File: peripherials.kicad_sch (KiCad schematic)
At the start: 58 parts, among them U15 PN7160AHN

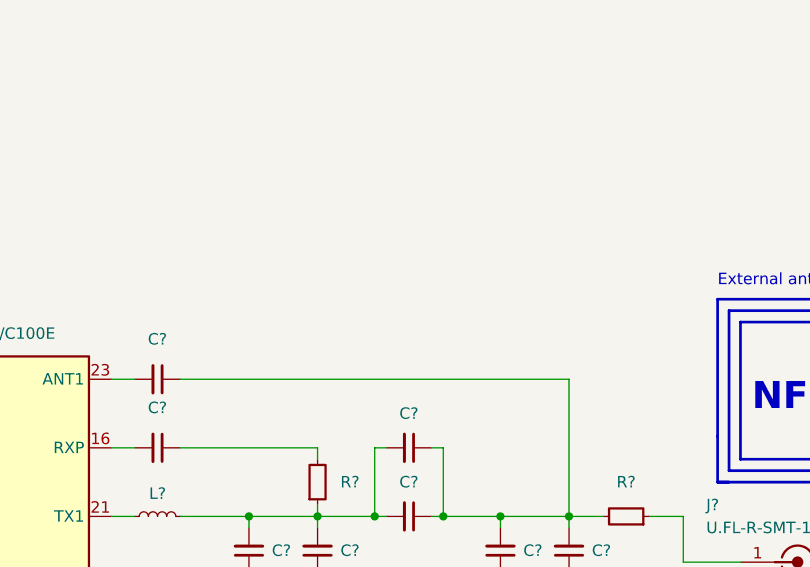
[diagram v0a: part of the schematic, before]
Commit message: [#54617] NFC: mark matching network as DNP & add note about it
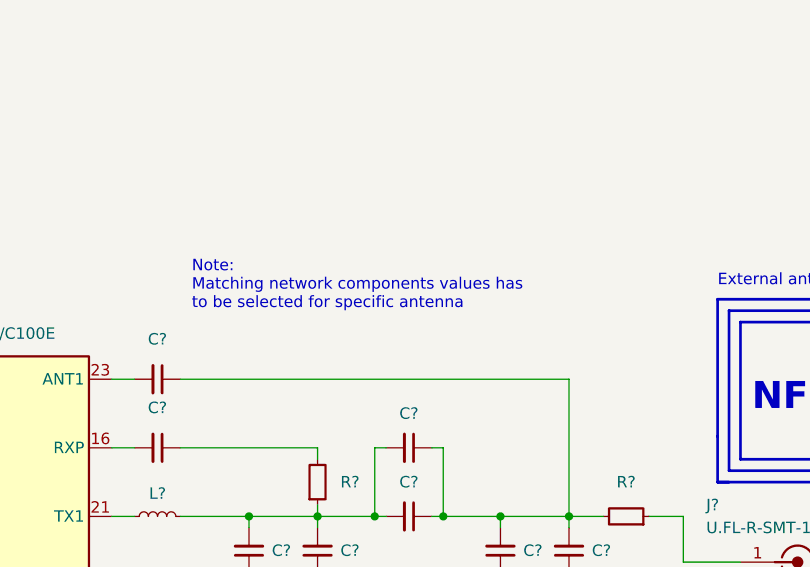
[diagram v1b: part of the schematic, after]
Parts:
- C? (x16), R? (x4): DNP (none) -> DNP
- L? (x2): footprint antmicro-footprints:L_0402_1005Metric -> antmicro-footprints:L_0603_1608Metric
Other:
- note added: "Note: Matching network components values has to be selected for specific antenna"
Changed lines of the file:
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@@
     (effects (font (size 1.27 1.27)) (justify left bottom))
   )
+  (text "Note:\nMatching network components values has \nto be selected for specific antenna"
+    (at 316.23 85.09 0)
+    (effects (font (size 1.27 1.27)) (justify left bottom))
+  )
   (text "GPIO connector" (at 19.05 153.67 0)
     (effects (font (size 2.9972 2.9972) (thickness 0.5994) bold) (justify left bottom))
@@
       (effects (font (size 1.27 1.27)) (justify left bottom) hide)
     )
+    (property "DNP" "DNP" (id 10) (at 367.03 123.19 0)
+      (effects (font (size 1.27 1.27)) hide)
+    )
     (pin "1")
     (pin "2")
@@
       (effects (font (size 1.27 1.27)) (justify left bottom) hide)
     )
+    (property "DNP" "DNP" (id 11) (at 342.9 100.33 0)
+      (effects (font (size 1.27 1.27)) hide)
+    )
     (pin "1")
     (pin "2")
@@
       (effects (font (size 1.27 1.27)) (justify left bottom) hide)
     )
+    (property "DNP" "DNP" (id 11) (at 342.9 107.95 0)
+      (effects (font (size 1.27 1.27)) hide)
+    )
     (pin "1")
     (pin "2")
@@
       (effects (font (size 1.27 1.27)) (justify left bottom) hide)
     )
+    (property "DNP" "DNP" (id 11) (at 322.58 121.92 0)
+      (effects (font (size 1.27 1.27)) hide)
+    )
     (pin "1")
     (pin "2")
@@
       (effects (font (size 1.27 1.27)) (justify left bottom) hide)
     )
+    (property "DNP" "DNP" (id 11) (at 342.9 130.81 0)
+      (effects (font (size 1.27 1.27)) hide)
+    )
     (pin "1")
     (pin "2")
@@
       (effects (font (size 1.27 1.27)) (justify left bottom) hide)
     )
+    (property "DNP" "DNP" (id 10) (at 330.2 106.68 0)
+      (effects (font (size 1.27 1.27)) hide)
+    )
     (pin "1")
     (pin "2")
@@
       (effects (font (size 1.27 1.27)) (justify left bottom) hide)
     )
+    (property "DNP" "DNP" (id 11) (at 330.2 114.3 0)
+      (effects (font (size 1.27 1.27)) hide)
+    )
     (pin "1")
     (pin "2")
@@
       (effects (font (size 1.27 1.27) (thickness 0.15)) (justify left bottom) hide)
     )
-    (property "Footprint" "antmicro-footprints:L_0402_1005Metric" (id 2) (at 323.85 130.81 0)
+    (property "Footprint" "antmicro-footprints:L_0603_1608Metric" (id 2) (at 323.85 130.81 0)
       (effects (font (size 1.27 1.27) (thickness 0.15)) (justify left bottom) hide)
     )
@@
       (effects (font (size 1.27 1.27)) (justify left bottom) hide)
     )
+    (property "DNP" "DNP" (id 11) (at 314.96 92.71 0)
+      (effects (font (size 1.27 1.27)) hide)
+    )
     (pin "1")
     (pin "2")
@@
       (effects (font (size 1.27 1.27)) (justify left bottom) hide)
     )
+    (property "DNP" "DNP" (id 11) (at 330.2 121.92 0)
+      (effects (font (size 1.27 1.27)) hide)
+    )
     (pin "1")
     (pin "2")
@@
       (effects (font (size 1.27 1.27)) (justify left bottom) hide)
     )
+    (property "DNP" "DNP" (id 11) (at 358.14 121.92 0)
+      (effects (font (size 1.27 1.27)) hide)
+    )
     (pin "1")
     (pin "2")
@@
       (effects (font (size 1.27 1.27)) (justify left bottom) hide)
     )
+    (property "DNP" "DNP" (id 10) (at 367.03 107.95 0)
+      (effects (font (size 1.27 1.27)) hide)
+    )
     (pin "1")
     (pin "2")
@@
       (effects (font (size 1.27 1.27) (thickness 0.15)) (justify left bottom) hide)
     )
-    (property "Footprint" "antmicro-footprints:L_0402_1005Metric" (id 2) (at 323.85 115.57 0)
+    (property "Footprint" "antmicro-footprints:L_0603_1608Metric" (id 2) (at 323.85 115.57 0)
       (effects (font (size 1.27 1.27) (thickness 0.15)) (justify left bottom) hide)
     )
@@
       (effects (font (size 1.27 1.27)) (justify left bottom) hide)
     )
+    (property "DNP" "DNP" (id 11) (at 314.96 138.43 0)
+      (effects (font (size 1.27 1.27)) hide)
+    )
     (pin "1")
     (pin "2")
@@
       (effects (font (size 1.27 1.27)) (justify left bottom) hide)
     )
+    (property "DNP" "DNP" (id 11) (at 350.52 121.92 0)
+      (effects (font (size 1.27 1.27)) hide)
+    )
     (pin "1")
     (pin "2")
@@
       (effects (font (size 1.27 1.27)) (justify left bottom) hide)
     )
+    (property "DNP" "DNP" (id 11) (at 314.96 130.81 0)
+      (effects (font (size 1.27 1.27)) hide)
+    )
     (pin "1")
     (pin "2")
@@
       (effects (font (size 1.27 1.27)) (justify left bottom) hide)
     )
+    (property "DNP" "DNP" (id 10) (at 330.2 124.46 0)
+      (effects (font (size 1.27 1.27)) hide)
+    )
     (pin "1")
     (pin "2")
@@
       (effects (font (size 1.27 1.27)) (justify left bottom) hide)
     )
+    (property "DNP" "DNP" (id 11) (at 358.14 114.3 0)
+      (effects (font (size 1.27 1.27)) hide)
+    )
     (pin "1")
     (pin "2")
@@
       (effects (font (size 1.27 1.27)) (justify left bottom) hide)
     )
+    (property "DNP" "DNP" (id 11) (at 342.9 123.19 0)
+      (effects (font (size 1.27 1.27)) hide)
+    )
     (pin "1")
     (pin "2")
@@
       (effects (font (size 1.27 1.27)) (justify left bottom) hide)
     )
+    (property "DNP" "DNP" (id 11) (at 314.96 100.33 0)
+      (effects (font (size 1.27 1.27)) hide)
+    )
     (pin "1")
     (pin "2")
@@
       (effects (font (size 1.27 1.27)) (justify left bottom) hide)
     )
+    (property "DNP" "DNP" (id 11) (at 350.52 114.3 0)
+      (effects (font (size 1.27 1.27)) hide)
+    )
     (pin "1")
     (pin "2")
@@
       (effects (font (size 1.27 1.27)) (justify left bottom) hide)
     )
+    (property "DNP" "DNP" (id 11) (at 322.58 114.3 0)
+      (effects (font (size 1.27 1.27)) hide)
+    )
     (pin "1")

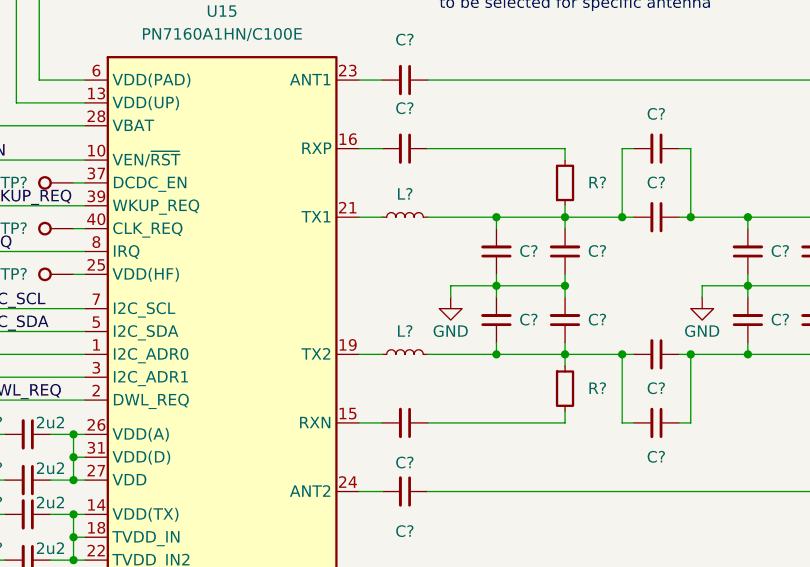
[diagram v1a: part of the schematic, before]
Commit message: [#54617] Migrate to KiCad 7
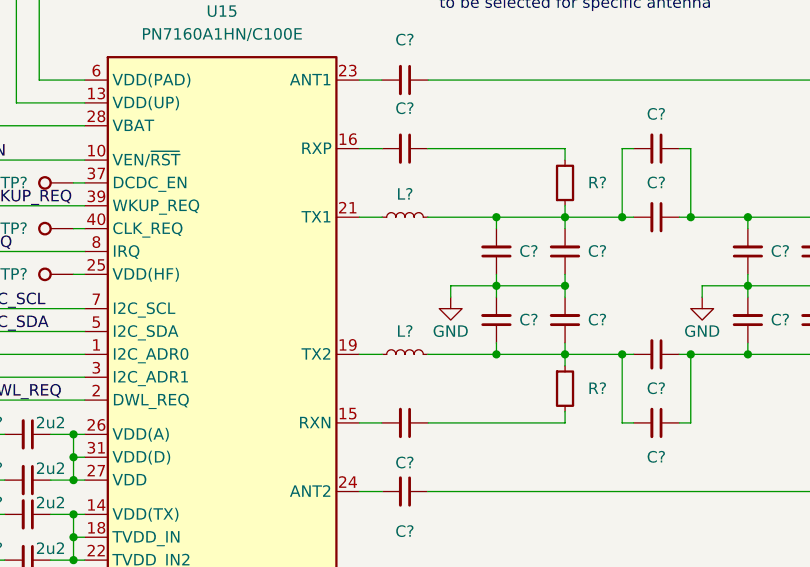
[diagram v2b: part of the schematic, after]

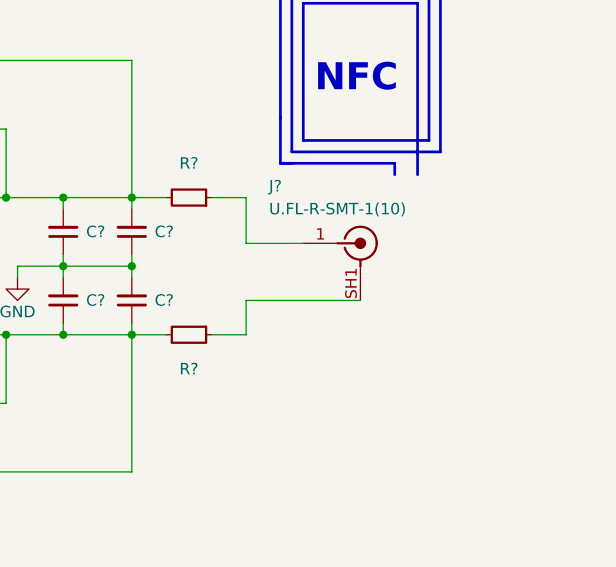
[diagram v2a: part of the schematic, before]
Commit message: [#54617] Move LVDS display related components to separate repo
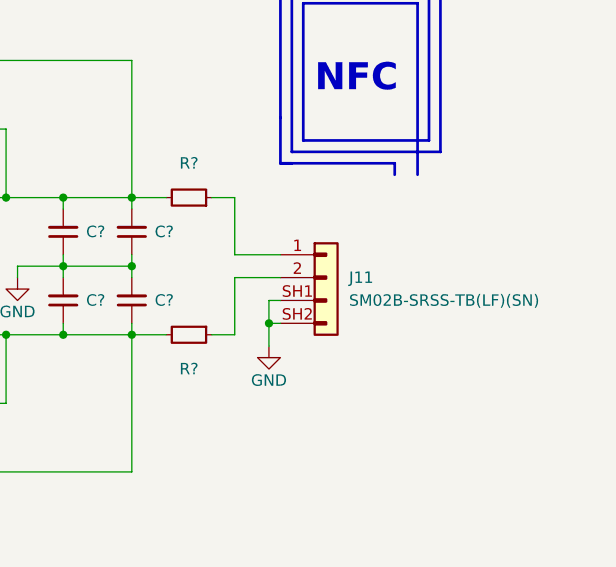
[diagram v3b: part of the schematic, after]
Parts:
- removed J?: U_FL-R-SMT-1, antmicro-footprints:Coax_Conn_U.FL, symbol antmicroCoaxialConnectorsRF:U_FL-R-SMT-1
- added J11: JST_SH_1x2_SM02B-SRSS-TB-LF-SN, antmicro-footprints:Conn_JST_SH_1x2_SM02B-SRSS-TB-LF-SN, symbol antmicroWire2BoardConnectors:JST_SH_1x2_SM02B-SRSS-TB-LF-SN
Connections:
- net GND: now also J11.SH1, J11.SH2
- net at R?.1: now also J11.2
- net at R?.1: now also J11.1
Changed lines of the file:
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@@
   (junction (at 106.68 50.8) (diameter 0) (color 0 0 0 0)
   )
+  (junction (at 373.38 121.92) (diameter 0) (color 0 0 0 0)
+  )
   (junction (at 151.13 49.53) (diameter 0) (color 0 0 0 0)
   )
@@
     (stroke (width 0) (type default))
   )
-  (wire (pts (xy 370.84 113.03) (xy 377.19 113.03))
+  (wire (pts (xy 369.57 114.3) (xy 374.65 114.3))
     (stroke (width 0) (type default))
   )
@@
     (stroke (width 0) (type default))
   )
+  (wire (pts (xy 373.38 121.92) (xy 373.38 124.46))
+    (stroke (width 0) (type default))
+  )
   (bus (pts (xy 76.2 168.91) (xy 24.13 168.91))
     (stroke (width 0) (type default))
@@
     (stroke (width 0) (type default))
   )
-  (wire (pts (xy 367.03 123.19) (xy 370.84 123.19))
+  (wire (pts (xy 374.65 119.38) (xy 373.38 119.38))
+    (stroke (width 0) (type default))
+  )
+  (wire (pts (xy 367.03 123.19) (xy 369.57 123.19))
     (stroke (width 0) (type default))
   )
@@
     (stroke (width 0) (type default))
   )
-  (wire (pts (xy 370.84 107.95) (xy 370.84 113.03))
+  (wire (pts (xy 369.57 107.95) (xy 369.57 114.3))
     (stroke (width 0) (type default))
   )
@@
     (stroke (width 0) (type default))
   )
+  (wire (pts (xy 373.38 119.38) (xy 373.38 121.92))
+    (stroke (width 0) (type default))
+  )
   (bus (pts (xy 111.76 185.42) (xy 111.76 187.96))
     (stroke (width 0) (type default))
@@
     (stroke (width 0) (type default))
   )
-  (wire (pts (xy 370.84 123.19) (xy 370.84 119.38))
+  (wire (pts (xy 369.57 123.19) (xy 369.57 116.84))
     (stroke (width 0) (type default))
   )
@@
     (stroke (width 0) (type default))
   )
+  (wire (pts (xy 373.38 121.92) (xy 374.65 121.92))
+    (stroke (width 0) (type default))
+  )
   (bus (pts (xy 24.13 168.91) (xy 24.13 179.07))
     (stroke (width 0) (type default))
@@
     (stroke (width 0) (type default))
   )
-  (wire (pts (xy 370.84 119.38) (xy 383.54 119.38))
+  (wire (pts (xy 369.57 116.84) (xy 374.65 116.84))
     (stroke (width 0) (type default))
   )
@@
     (stroke (width 0) (type default))
   )
-  (wire (pts (xy 367.03 107.95) (xy 370.84 107.95))
+  (wire (pts (xy 367.03 107.95) (xy 369.57 107.95))
     (stroke (width 0) (type default))
   )
@@
     )
   )
-  (symbol (lib_id "antmicroCoaxialConnectorsRF:U_FL-R-SMT-1") (at 377.19 113.03 0) (unit 1)
-    (in_bom yes) (on_board yes) (dnp no)
-    (property "Reference" "J?" (at 373.38 106.68 0)
-      (effects (font (size 1.27 1.27) (thickness 0.15)) (justify left))
-    )
-    (property "Value" "U_FL-R-SMT-1" (at 397.51 120.65 0)
-      (effects (font (size 1.27 1.27) (thickness 0.15)) (justify left bottom) hide)
-    )
-    (property "Footprint" "antmicro-footprints:Coax_Conn_U.FL" (at 397.51 123.19 0)
-      (effects (font (size 1.27 1.27) (thickness 0.15)) (justify left bottom) hide)
-    )
-    (property "Datasheet" "https://media.digikey.com/pdf/Data%20Sheets/Hirose%20PDFs/UFL%20Series.pdf" (at 397.51 125.73 0)
-      (effects (font (size 1.27 1.27) (thickness 0.15)) (justify left bottom) hide)
-    )
-    (property "MPN" "U.FL-R-SMT-1(10)" (at 373.38 109.22 0)
-      (effects (font (size 1.27 1.27) (thickness 0.15)) (justify left))
-    )
-    (property "Manufacturer" "Hirose Electric" (at 397.51 128.27 0)
-      (effects (font (size 1.27 1.27) (thickness 0.15)) (justify left bottom) hide)
-    )
-    (property "Author" "Antmicro" (at 397.51 130.81 0)
-      (effects (font (size 1.27 1.27) (thickness 0.15)) (justify left bottom) hide)
-    )
-    (property "License" "Apache-2.0" (at 397.51 133.35 0)
-      (effects (font (size 1.27 1.27) (thickness 0.15)) (justify left bottom) hide)
-    )
-    (pin "1")
-    (pin "SH1")
-    (pin "SH2")
-    (instances
-      (project "cm4-baseboard"
-        (path "/60b842dc-0853-4a25-99ac-5784ddf94d0d/db597aea-6022-4be8-a5d9-f0f6712c4ff6"
-          (reference "J?") (unit 1)
-        )
-      )
-    )
-  )
   (symbol (lib_id "antmicroCapacitors0402:C_4u7_0402") (at 248.92 87.63 90) (unit 1)
     (in_bom yes) (on_board yes) (dnp no)
@@
     )
   )
+  (symbol (lib_id "antmicropower:GND") (at 373.38 124.46 0) (unit 1)
+    (in_bom yes) (on_board yes) (dnp no)
+    (property "Reference" "#PWR03" (at 382.27 127 0)
+      (effects (font (size 1.27 1.27) (thickness 0.15)) (justify left bottom) hide)
+    )
+    (property "Value" "GND" (at 373.38 128.27 0)
+      (effects (font (size 1.27 1.27) (thickness 0.15)))
+    )
+    (property "Footprint" "" (at 382.27 132.08 0)
+      (effects (font (size 1.27 1.27) (thickness 0.15)) (justify left bottom) hide)
+    )
+    (property "Datasheet" "" (at 382.27 137.16 0)
+      (effects (font (size 1.27 1.27) (thickness 0.15)) (justify left bottom) hide)
+    )
+    (property "Author" "Antmicro" (at 382.27 132.08 0)
+      (effects (font (size 1.27 1.27) (thickness 0.15)) (justify left bottom) hide)
+    )
+    (property "License" "Apache-2.0" (at 382.27 134.62 0)
+      (effects (font (size 1.27 1.27) (thickness 0.15)) (justify left bottom) hide)
+    )
+    (pin "1")
+    (instances
+      (project "cm4-baseboard"
+        (path "/60b842dc-0853-4a25-99ac-5784ddf94d0d/db597aea-6022-4be8-a5d9-f0f6712c4ff6"
+          (reference "#PWR03") (unit 1)
+        )
+      )
+    )
+  )
   (symbol (lib_id "antmicroResistors0402:R_10k_0402") (at 236.22 132.08 90) (unit 1)
     (in_bom yes) (on_board yes) (dnp no)
@@
         )
       )
+    )
+  )
+  (symbol (lib_id "antmicroWire2BoardConnectors:JST_SH_1x2_SM02B-SRSS-TB-LF-SN") (at 374.65 114.3 0) (unit 1)
+    (in_bom yes) (on_board yes) (dnp no)
+    (property "Reference" "J11" (at 382.27 116.84 0)
+      (effects (font (size 1.27 1.27) (thickness 0.15)) (justify left))
+    )
+    (property "Value" "JST_SH_1x2_SM02B-SRSS-TB-LF-SN" (at 401.32 120.65 0)
+      (effects (font (size 1.27 1.27) (thickness 0.15)) (justify left bottom) hide)
+    )
+    (property "Footprint" "antmicro-footprints:Conn_JST_SH_1x2_SM02B-SRSS-TB-LF-SN" (at 401.32 123.19 0)
+      (effects (font (size 1.27 1.27) (thickness 0.15)) (justify left bottom) hide)
+    )
+    (property "Datasheet" "https://www.jst-mfg.com/product/pdf/eng/eSH.pdf" (at 401.32 125.73 0)
+      (effects (font (size 1.27 1.27) (thickness 0.15)) (justify left bottom) hide)
+    )
+    (property "MPN" "SM02B-SRSS-TB(LF)(SN)" (at 382.27 119.38 0)
+      (effects (font (size 1.27 1.27) (thickness 0.15)) (justify left))
+    )
+    (property "Manufacturer" "JST Automotive Connectors" (at 401.32 130.81 0)
+      (effects (font (size 1.27 1.27) (thickness 0.15)) (justify left bottom) hide)
+    )
+    (property "Author" "Antmicro" (at 401.32 133.35 0)
+      (effects (font (size 1.27 1.27) (thickness 0.15)) (justify left bottom) hide)
+    )
+    (property "License" "Apache-2.0" (at 401.32 135.89 0)
+      (effects (font (size 1.27 1.27) (thickness 0.15)) (justify left bottom) hide)
+    )
+    (pin "SH1")
+    (pin "1")
+    (pin "SH2")
+    (pin "2")
+    (instances
+      (project "cm4-baseboard"
+        (path "/60b842dc-0853-4a25-99ac-5784ddf94d0d/db597aea-6022-4be8-a5d9-f0f6712c4ff6"
+          (reference "J11") (unit 1)
+        )
+      )
